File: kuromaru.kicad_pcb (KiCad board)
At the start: 2 copper layers, 134 x 95.1 mm, 78 parts, among them J1 USB_C_Receptacle_USB2.0, J108 Conn_01x01_Female, J109 Conn_01x01_Female, J5 Conn_01x02, SW1 SW_Push, SW101 SW_Push, SW102 SW_Push, SW103 SW_Push, SW104 SW_Push, SW105 SW_Push, SW106 SW_Push, SW107 SW_Push, SW108 SW_Push, SW109 SW_Push, SW110 SW_SPST_TL3342, SW112 SW_Push, SW113 SW_Push, SW114 SW_Push, SW115 SW_Push, SW116 SW_Push, SW117 SW_Push, SW118 SW_Push, SW119 locked, SW2 SW_Push, U1 RP2040, U2 GD25Q80CEIGR, U3 XC6210B332MR-G, Y1 Crystal_GND24

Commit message: Before diodeless design
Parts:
- removed J108, J109: Conn_01x01_Female, Connector_Wire:SolderWirePad_1x01_SMD_1x2mm
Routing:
- net rgb_l: track 7.18 -> 4.99 mm, vias 1 -> 0
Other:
- board text removed: "0"
- board text removed: "GPIO"

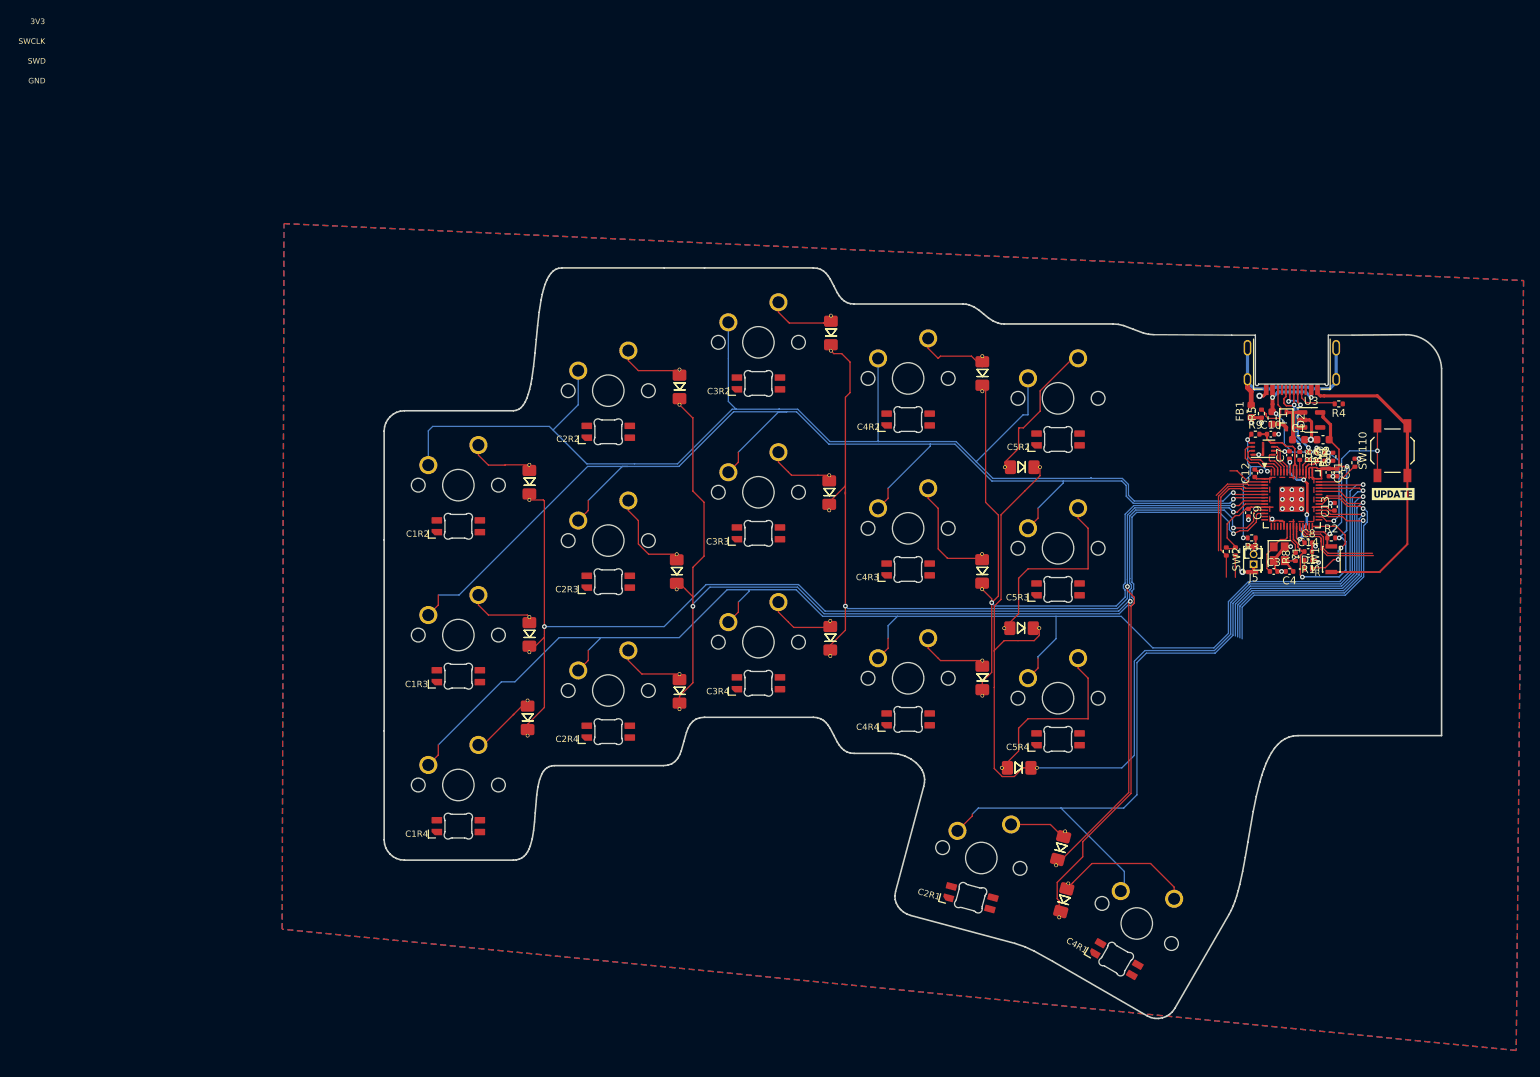
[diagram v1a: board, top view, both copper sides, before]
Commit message: Update to diodeless
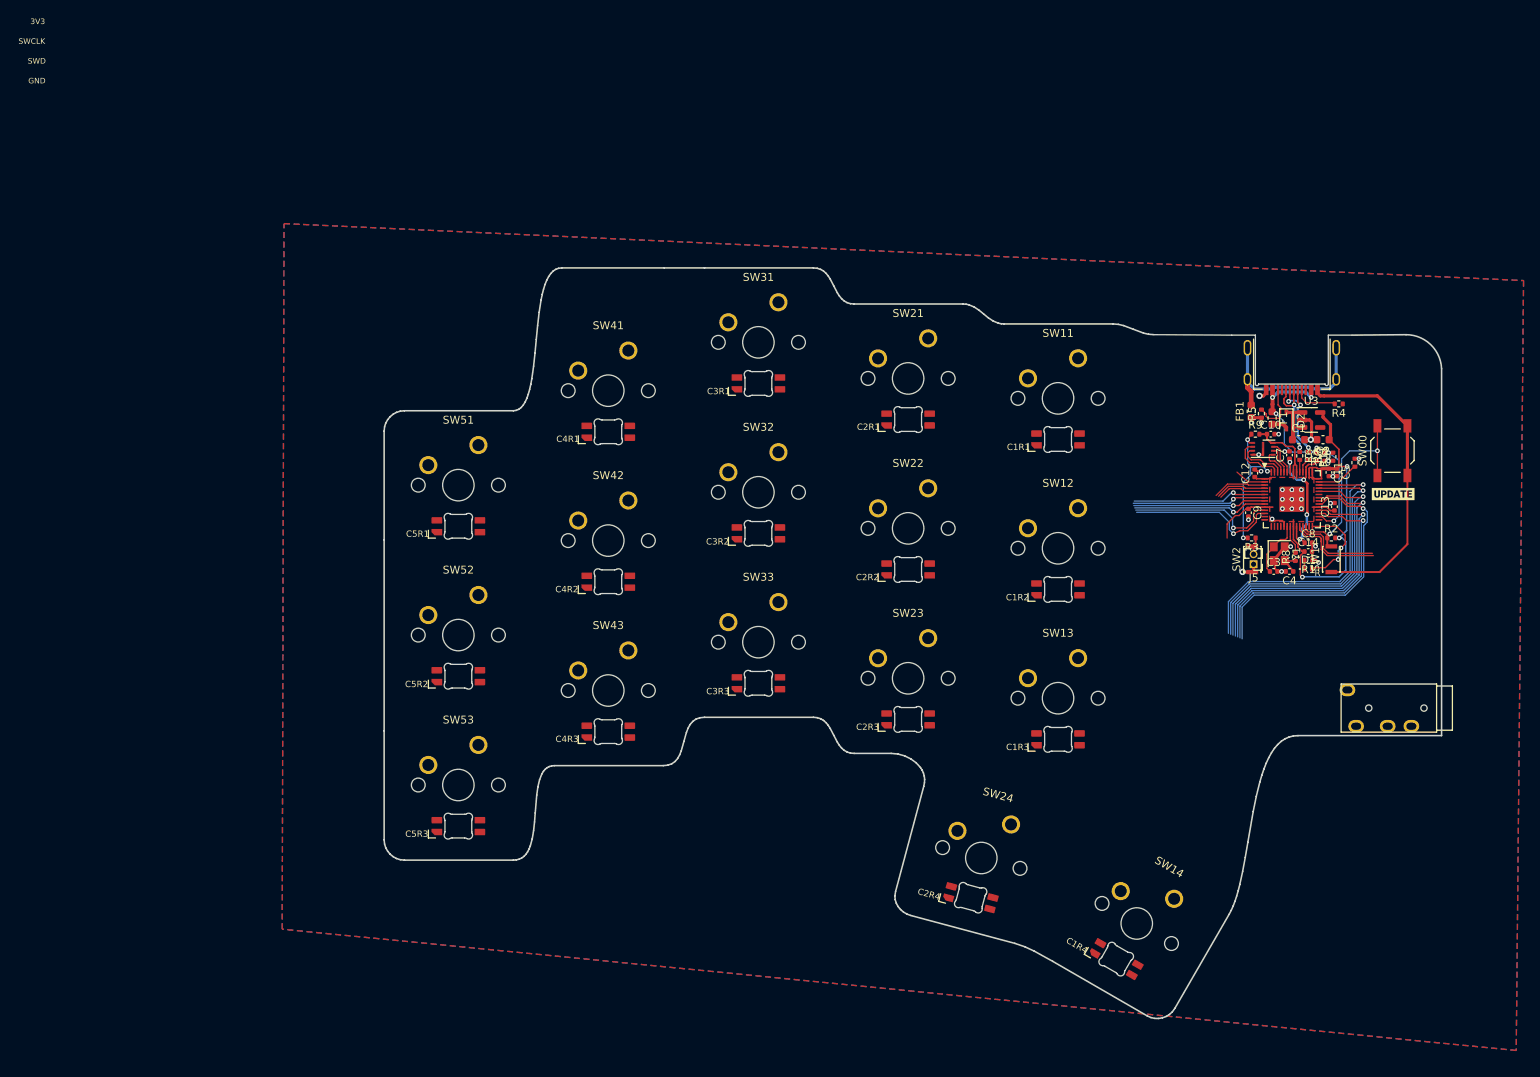
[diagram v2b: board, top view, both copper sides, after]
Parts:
- removed D101, D102, D103, D104, D105, D106, D107, D108, D109, D110, D111, D112, D113, D114, D115, D116, D117: D, local-libraries:D_1206_handsolder_reversible
- removed R103, R104: 4.7k, local-libraries:R_0402_1005Metric_nolabel
- added J102: Serial, keebio:TRRS-PJ-320A-no-Fmask, F.Cu at (177.4, 82.0)
- SW00: renamed from SW110; value SW_SPST_TL3342 -> SW_SPST
- SW11: renamed from SW115; value SW_Push -> SW_Push_SK6812
- SW12: renamed from SW116; value SW_Push -> SW_Push_SK6812
- SW13: renamed from SW117; value SW_Push -> SW_Push_SK6812
- SW21: renamed from SW112; value SW_Push -> SW_Push_SK6812
- SW22: renamed from SW113; value SW_Push -> SW_Push_SK6812
- SW23: renamed from SW114; value SW_Push -> SW_Push_SK6812
- SW24: renamed from SW118; value SW_Push -> SW_Push_SK6812
- SW31: renamed from SW107; value SW_Push -> SW_Push_SK6812
- SW32: renamed from SW108; value SW_Push -> SW_Push_SK6812
- SW33: renamed from SW109; value SW_Push -> SW_Push_SK6812
- SW41: renamed from SW104; value SW_Push -> SW_Push_SK6812
- SW42: renamed from SW105; value SW_Push -> SW_Push_SK6812
- SW43: renamed from SW106; value SW_Push -> SW_Push_SK6812
- SW51: renamed from SW101; value SW_Push -> SW_Push_SK6812
- SW52: renamed from SW102; value SW_Push -> SW_Push_SK6812
- SW53: renamed from SW103; value SW_Push -> SW_Push_SK6812
- renumbered SW119 to SW14
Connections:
- net NCS renamed /D21
- net miso_l renamed /MISO
- net mosi_l renamed /MOSI
- net rgb_l renamed rgb_din
- net sc_l renamed /SCLK
- net serial_l renamed serial_tx
- C1 pad 1: bat_l -> +5V
- C1 pad 2: Gnd_l -> GND
- C10 pad 2: Gnd_l -> GND
- C11 pad 2: Gnd_l -> GND
- C12 pad 2: Gnd_l -> GND
- C13 pad 2: Gnd_l -> GND
- C14 pad 2: Gnd_l -> GND
- C2 pad 2: Gnd_l -> GND
- C3 pad 2: Gnd_l -> GND
- C4 pad 2: Gnd_l -> GND
- C5 pad 2: Gnd_l -> GND
- C6 pad 2: Gnd_l -> GND
- C7 pad 2: Gnd_l -> GND
- C8 pad 2: Gnd_l -> GND
- C9 pad 2: Gnd_l -> GND
- D2 pad 1: bat_l -> +5V
- FB1 pad 1: Gnd_l -> GND
- J1 pad A1: Gnd_l -> GND
- J1 pad A12: Gnd_l -> GND
- J1 pad B1: Gnd_l -> GND
- J1 pad B12: Gnd_l -> GND
- J5 pad 1: Gnd_l -> GND
- R1 pad 1: Gnd_l -> GND
- R101 pad 2: Net-(JP111-Pad1) -> unconnected-(R101-Pad2)
- R11 pad 1: Gnd_l -> GND
- R4 pad 1: Gnd_l -> GND
- R5 pad 1: Gnd_l -> GND
- SW1 pad 1: Gnd_l -> unconnected-(SW1-Pad1)
- SW1 pad 2: Rst_l -> unconnected-(SW1-Pad2)
- SW11 pad 1: row2_l -> +5V
- SW11 pad 2: Net-(D113-Pad2) -> Net-(SW52-Pad4)
- SW11 pad 3: (no net) -> GND
- SW11 pad 4: (no net) -> Net-(SW11-Pad4)
- SW11 pad 5: (no net) -> GND
- SW11 pad 6: (no net) -> switch11
- SW12 pad 1: row3_l -> +5V
- SW12 pad 2: Net-(D114-Pad2) -> Net-(SW53-Pad4)
- SW12 pad 3: (no net) -> GND
- SW12 pad 4: (no net) -> Net-(SW12-Pad4)
- SW12 pad 5: (no net) -> GND
- SW12 pad 6: (no net) -> switch12
- SW13 pad 1: row4_l -> +5V
- SW13 pad 2: Net-(D115-Pad2) -> Net-(SW24-Pad4)
- SW13 pad 3: (no net) -> GND
- SW13 pad 4: (no net) -> Net-(SW13-Pad4)
- SW13 pad 5: (no net) -> GND
- SW13 pad 6: (no net) -> switch13
- SW14 pad 1: row1_l -> +5V
- SW14 pad 2: Net-(D117-Pad2) -> unconnected-(SW14-Pad2)
- SW14 pad 3: (no net) -> GND
- SW14 pad 4: (no net) -> Net-(SW14-Pad4)
- SW14 pad 5: (no net) -> GND
- SW14 pad 6: (no net) -> switch14
- SW2 pad 1: Gnd_l -> unconnected-(SW2-Pad1)
- SW2 pad 2: Net-(J5-Pad2) -> unconnected-(SW2-Pad2)
- SW21 pad 1: row2_l -> +5V
- SW21 pad 2: Net-(D110-Pad2) -> Net-(SW11-Pad4)
- SW21 pad 3: (no net) -> GND
- SW21 pad 4: (no net) -> Net-(SW21-Pad4)
- SW21 pad 5: (no net) -> GND
- SW21 pad 6: (no net) -> switch21
- SW22 pad 1: row3_l -> +5V
- SW22 pad 2: Net-(D111-Pad2) -> Net-(SW12-Pad4)
- SW22 pad 3: (no net) -> GND
- SW22 pad 4: (no net) -> Net-(SW22-Pad4)
- SW22 pad 5: (no net) -> GND
- SW22 pad 6: (no net) -> switch22
- SW23 pad 1: row4_l -> +5V
- SW23 pad 2: Net-(D112-Pad2) -> Net-(SW13-Pad4)
- SW23 pad 3: (no net) -> GND
- SW23 pad 4: (no net) -> Net-(SW23-Pad4)
- SW23 pad 5: (no net) -> GND
- SW23 pad 6: (no net) -> switch23
- SW24 pad 1: row1_l -> +5V
- SW24 pad 2: Net-(D116-Pad2) -> Net-(SW14-Pad4)
- SW24 pad 3: (no net) -> GND
- SW24 pad 4: (no net) -> Net-(SW24-Pad4)
- SW24 pad 5: (no net) -> GND
- SW24 pad 6: (no net) -> switch24
- SW31 pad 1: row2_l -> +5V
- SW31 pad 2: Net-(D107-Pad2) -> Net-(SW21-Pad4)
- SW31 pad 3: (no net) -> GND
- SW31 pad 4: (no net) -> Net-(SW31-Pad4)
- SW31 pad 5: (no net) -> GND
- SW31 pad 6: (no net) -> switch31
- SW32 pad 1: row3_l -> +5V
- SW32 pad 2: Net-(D108-Pad2) -> Net-(SW22-Pad4)
- SW32 pad 3: (no net) -> GND
- SW32 pad 4: (no net) -> Net-(SW32-Pad4)
- SW32 pad 5: (no net) -> GND
- SW32 pad 6: (no net) -> switch32
- SW33 pad 1: row4_l -> +5V
- SW33 pad 2: Net-(D109-Pad2) -> Net-(SW23-Pad4)
- SW33 pad 3: (no net) -> GND
- SW33 pad 4: (no net) -> Net-(SW33-Pad4)
- SW33 pad 5: (no net) -> GND
- SW33 pad 6: (no net) -> switch33
- SW41 pad 1: row2_l -> +5V
- SW41 pad 2: Net-(D104-Pad2) -> Net-(SW31-Pad4)
- SW41 pad 3: (no net) -> GND
- SW41 pad 4: (no net) -> Net-(SW41-Pad4)
- SW41 pad 5: (no net) -> GND
- SW41 pad 6: (no net) -> switch41
- SW42 pad 1: row3_l -> +5V
- SW42 pad 2: Net-(D105-Pad2) -> Net-(SW32-Pad4)
- SW42 pad 3: (no net) -> GND
- SW42 pad 4: (no net) -> Net-(SW42-Pad4)
- SW42 pad 5: (no net) -> GND
- SW42 pad 6: (no net) -> switch42
- SW43 pad 1: row4_l -> +5V
- SW43 pad 2: Net-(D106-Pad2) -> Net-(SW33-Pad4)
- SW43 pad 3: (no net) -> GND
- SW43 pad 4: (no net) -> Net-(SW53-Pad2)
- SW43 pad 5: (no net) -> GND
- SW43 pad 6: (no net) -> switch43
- SW51 pad 1: row2_l -> +5V
- SW51 pad 2: Net-(D101-Pad2) -> Net-(SW41-Pad4)
- SW51 pad 3: (no net) -> GND
- SW51 pad 4: (no net) -> Net-(SW51-Pad4)
- SW51 pad 5: (no net) -> GND
- SW51 pad 6: (no net) -> switch51
- SW52 pad 1: row3_l -> +5V
- SW52 pad 2: Net-(D102-Pad2) -> Net-(SW42-Pad4)
- SW52 pad 3: (no net) -> GND
- SW52 pad 4: (no net) -> Net-(SW52-Pad4)
- SW52 pad 5: (no net) -> GND
- SW52 pad 6: (no net) -> switch52
- SW53 pad 1: row4_l -> +5V
- SW53 pad 2: Net-(D103-Pad2) -> Net-(SW53-Pad2)
- SW53 pad 3: (no net) -> GND
- SW53 pad 4: (no net) -> Net-(SW53-Pad4)
- SW53 pad 5: (no net) -> GND
- SW53 pad 6: (no net) -> switch53
- U1 pad 11: col1_l -> switch21
- U1 pad 12: col2_l -> switch22
- U1 pad 13: unconnected-(U1-Pad13) -> switch23
- U1 pad 14: unconnected-(U1-Pad14) -> switch24
- U1 pad 15: /D12 -> switch25
- U1 pad 16: /D13 -> switch21
- U1 pad 17: /D14 -> switch22
- U1 pad 18: /D15 -> switch23
- U1 pad 19: Gnd_l -> GND
- U1 pad 27: /D16 -> switch24
- U1 pad 29: unconnected-(U1-Pad29) -> switch25
- U1 pad 36: unconnected-(U1-Pad36) -> switch24
- U1 pad 37: unconnected-(U1-Pad37) -> switch25
- U1 pad 38: row1_l -> /A0
- U1 pad 39: col5_l -> /A1
- U1 pad 4: sda_l -> serial_rx
- U1 pad 40: row4_l -> /A2
- U1 pad 41: hand -> /A3
- U1 pad 5: scl_l -> switch11
- U1 pad 57: Gnd_l -> GND
- U1 pad 6: row2_l -> switch12
- U1 pad 7: row3_l -> switch13
- U1 pad 8: col4_l -> switch14
- U1 pad 9: col3_l -> switch15
- U2 pad 4: Gnd_l -> GND
- U2 pad 9: Gnd_l -> GND
- U3 pad 1: bat_l -> +5V
- U3 pad 2: Gnd_l -> GND
- U3 pad 3: bat_l -> +5V
- Y1 pad 2: Gnd_l -> GND
- Y1 pad 4: Gnd_l -> GND
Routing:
- net col1_l: track 182.8 -> 0.00 mm, vias 3 -> 0
- net row4_l: track 180.1 -> 0.00 mm, vias 1 -> 0
- net row2_l: track 166.4 -> 0.00 mm, vias 1 -> 0
- net row3_l: track 163.1 -> 0.00 mm, vias 1 -> 0
- net col3_l: track 157.7 -> 0.00 mm, vias 3 -> 0
- net col2_l: track 134.7 -> 0.00 mm, vias 2 -> 0
- net col5_l: track 130.9 -> 0.00 mm, vias 1 -> 0
- net row1_l: track 107.2 -> 0.00 mm, vias 1 -> 0
- net col4_l: track 90.3 -> 0.00 mm, vias 2 -> 0
- net Gnd_l: track 69.8 -> 0.00 mm, vias 27 -> 11
- net GND: track 0.00 -> 67.5 mm, vias 0 -> 15
- net /A2: track 0.00 -> 38.8 mm, vias 0 -> 1
- net /A1: track 0.00 -> 38.0 mm, vias 0 -> 1
- net /A0: track 0.00 -> 37.3 mm, vias 0 -> 1
- net Net-(D114-Pad2): track 24.6 -> 0.00 mm
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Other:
- board text added: "C1R1"
- board text added: "C3R1"
- board text added: "C5R1"
- board text removed: "C3R4"
- board text removed: "C4R4"
- board text removed: "C5R4"

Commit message: Rework controller, commit before splay
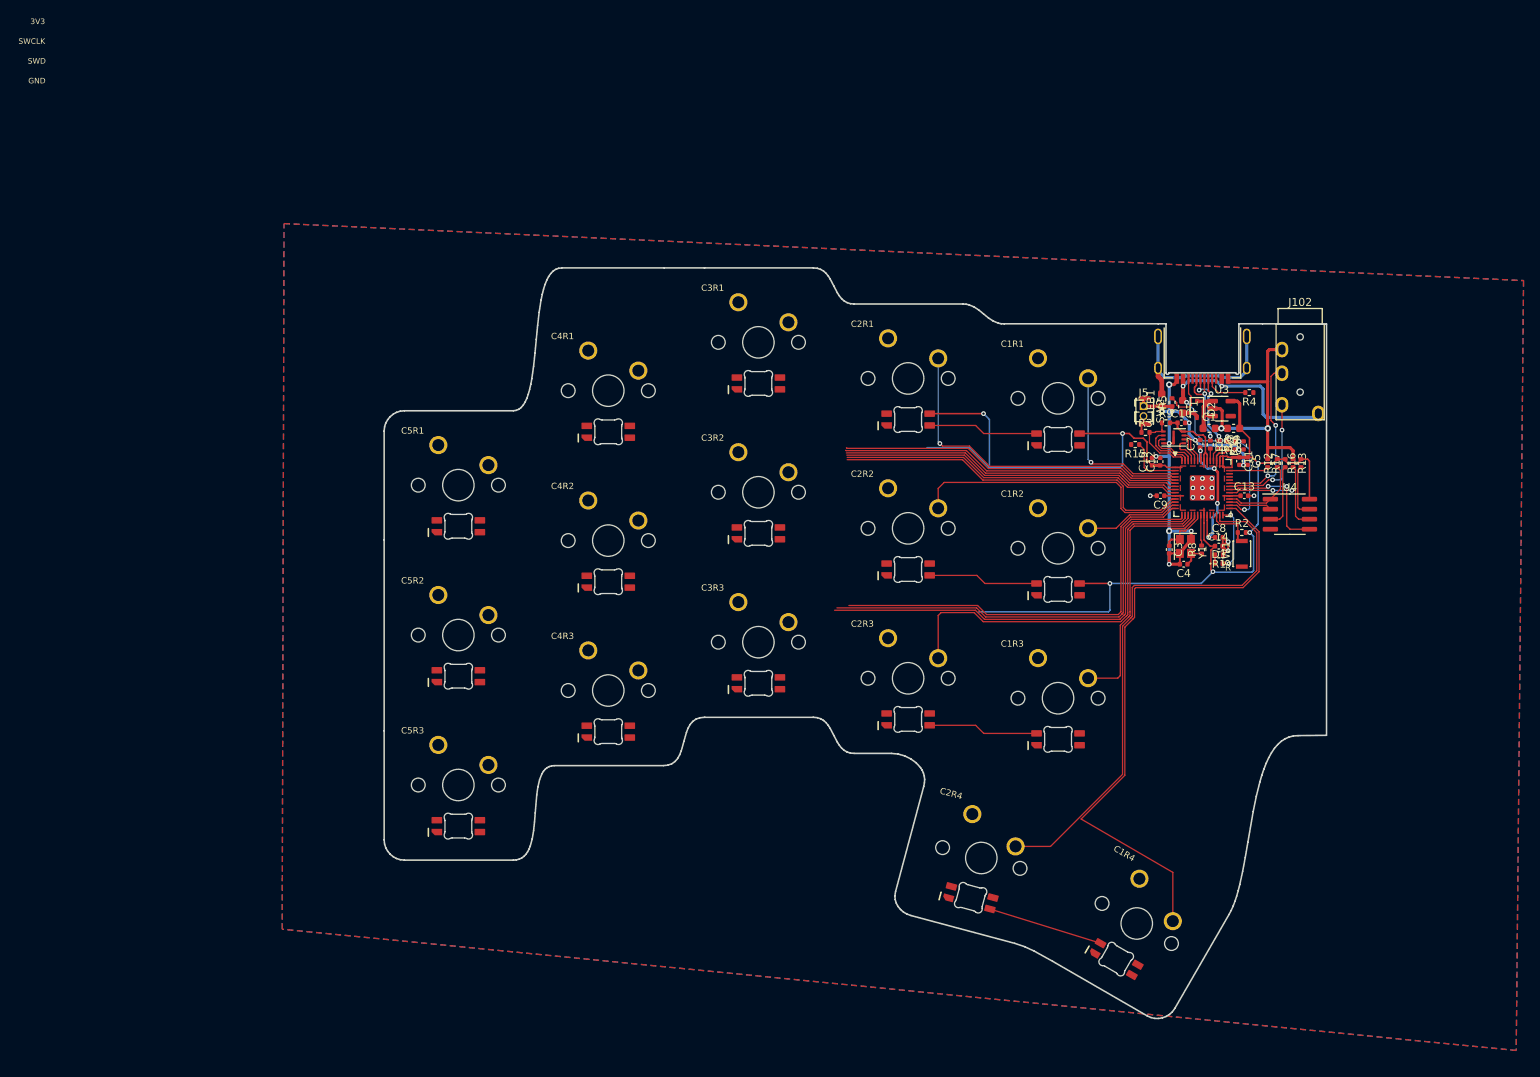
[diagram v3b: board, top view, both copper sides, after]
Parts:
- removed SW00: SW_SPST, Button_Switch_SMD:SW_SPST_TL3342
- removed kibuzzard-62C19A64: G***, kibuzzard-62C19A64
- added C15: 1µ, Capacitor_SMD:C_0402_1005Metric, F.Cu at (141.4, 50.8)
- added R12: 100k, Resistor_SMD:R_0402_1005Metric, F.Cu at (157.2, 51.0)
- added R13: 100k, Resistor_SMD:R_0402_1005Metric, F.Cu at (159.2, 51.0)
- added R15: 300, Resistor_SMD:R_0402_1005Metric, F.Cu at (139.2, 48.6)
- added R16: 5.1k, Resistor_SMD:R_0402_1005Metric, F.Cu at (160.2, 51.0)
- added R17: 5.1k, Resistor_SMD:R_0402_1005Metric, F.Cu at (158.2, 51.0)
- added U4: 25LCxxx, Package_SO:SOIC-8_3.9x4.9mm_P1.27mm, F.Cu at (158.8, 57.4)
- J102: footprint keebio:TRRS-PJ-320A-no-Fmask -> local-libraries:delay_TRRS_PJ_320A
- moved J102 46.9 mm to (160.1, 38.4), turned to 0 degrees
- moved J5 24.4 mm to (140.3, 43.7), turned to 0 degrees
- moved SW2 23.2 mm to (140.4, 44.4), turned to -90 degrees
- moved R3 19.0 mm to (140.5, 47.1), turned to 0 degrees
- moved C3 13.5 mm to (143.5, 61.9), turned to -90 degrees
- moved C4 13.4 mm to (145.3, 63.8)
- moved C12 12.1 mm to (142.4, 50.8)
- moved R8 11.9 mm to (147.6, 61.9)
- moved Y1 11.9 mm to (145.6, 61.5)
- moved C13 11.5 mm to (153.0, 55.1), turned to 0 degrees
- moved C1 11.4 mm to (148.6, 46.5)
- moved C2 11.4 mm to (151.7, 46.5)
- moved C6 11.4 mm to (151.4, 49.2)
- moved C7 11.4 mm to (147.4, 48.5)
- moved F1 11.4 mm to (145.2, 43.8)
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- renumbered SW11 to C1R1, SW12 to C1R2, SW13 to C1R3, SW14 to C1R4, SW21 to C2R1, SW22 to C2R2, SW23 to C2R3, SW24 to C2R4, SW31 to C3R1, SW32 to C3R2, SW33 to C3R3, SW41 to C4R1, SW42 to C4R2, SW43 to C4R3, SW51 to C5R1, SW52 to C5R2, SW53 to C5R3, R101 to R14
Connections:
- C1R1 pad 1: +5V -> +3V3
- C1R1 pad 6: switch11 -> switch_c1r1
- C1R2 pad 1: +5V -> +3V3
- C1R2 pad 6: switch12 -> switch_c1r2
- C1R3 pad 1: +5V -> +3V3
- C1R3 pad 6: switch13 -> switch_c1r3
- C1R4 pad 1: +5V -> +3V3
- C1R4 pad 6: switch14 -> switch_c1r4
- C2R1 pad 1: +5V -> +3V3
- C2R1 pad 6: switch21 -> switch_c2r1
- C2R2 pad 1: +5V -> +3V3
- C2R2 pad 6: switch22 -> switch_c2r2
- C2R3 pad 1: +5V -> +3V3
- C2R3 pad 6: switch23 -> switch_c2r3
- C2R4 pad 1: +5V -> +3V3
- C2R4 pad 6: switch24 -> switch_c2r4
- C3R1 pad 1: +5V -> +3V3
- C3R1 pad 6: switch31 -> switch_c3r1
- C3R2 pad 1: +5V -> +3V3
- C3R2 pad 6: switch32 -> switch_c3r2
- C3R3 pad 1: +5V -> +3V3
- C3R3 pad 6: switch33 -> switch_c3r3
- C4R1 pad 1: +5V -> +3V3
- C4R1 pad 6: switch41 -> switch_c4r1
- C4R2 pad 1: +5V -> +3V3
- C4R2 pad 6: switch42 -> switch_c4r2
- C4R3 pad 1: +5V -> +3V3
- C4R3 pad 6: switch43 -> switch_c4r3
- C5R1 pad 1: +5V -> +3V3
- C5R1 pad 6: switch51 -> switch_c5r1
- C5R2 pad 1: +5V -> +3V3
- C5R2 pad 6: switch52 -> switch_c5r2
- C5R3 pad 1: +5V -> +3V3
- C5R3 pad 6: switch53 -> switch_c5r3
- R14 pad 1: hand -> hands
- R14 pad 2: unconnected-(R101-Pad2) -> GND
- R2 pad 1: Rst_l -> reset
- SW1 pad 1: unconnected-(SW1-Pad1) -> GND
- SW1 pad 2: unconnected-(SW1-Pad2) -> reset
- SW2 pad 1: unconnected-(SW2-Pad1) -> GND
- SW2 pad 2: unconnected-(SW2-Pad2) -> Net-(J5-Pad2)
- U1 pad 11: switch21 -> switch_c3r2
- U1 pad 12: switch22 -> switch_c2r2
- U1 pad 13: switch23 -> switch_c1r2
- U1 pad 14: switch24 -> switch_c5r3
- U1 pad 15: switch25 -> switch_c4r3
- U1 pad 16: switch21 -> switch_c3r3
- U1 pad 17: switch22 -> switch_c2r3
- U1 pad 18: switch23 -> switch_c1r3
- U1 pad 26: Rst_l -> reset
- U1 pad 27: switch24 -> switch_c2r4
- U1 pad 29: switch25 -> switch_c1r4
- U1 pad 3: serial_tx -> switch_c1r1
- U1 pad 32: /D21 -> /EEPROM_CS
- U1 pad 36: switch24 -> serial_tx
- U1 pad 37: switch25 -> serial_rx
- U1 pad 4: serial_rx -> switch_c2r1
- U1 pad 41: /A3 -> hands
- U1 pad 5: switch11 -> switch_c3r1
- U1 pad 6: switch12 -> switch_c4r1
- U1 pad 7: switch13 -> switch_c5r1
- U1 pad 8: switch14 -> switch_c5r2
- U1 pad 9: switch15 -> switch_c4r2
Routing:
- net +3V3: track 72.2 -> 174.6 mm, vias 3 -> 6
- net switch_c1r4: track 0.00 -> 78.3 mm
- net switch_c2r4: track 0.00 -> 69.1 mm
- net switch_c3r3: track 0.00 -> 56.9 mm
- net switch_c4r3: track 0.00 -> 56.1 mm
- net switch_c5r3: track 0.00 -> 53.7 mm
- net switch_c2r3: track 0.00 -> 49.9 mm
- net GND: track 67.5 -> 114.3 mm, vias 15 -> 27
- net switch_c3r2: track 0.00 -> 46.4 mm
- net switch_c4r1: track 0.00 -> 43.5 mm
- net switch_c5r1: track 0.00 -> 43.4 mm
- net switch_c5r2: track 0.00 -> 43.4 mm
- net switch_c4r2: track 0.00 -> 43.4 mm
- net switch_c3r1: track 0.00 -> 43.4 mm
- net switch_c2r1: track 0.00 -> 42.5 mm, vias 0 -> 1
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- added copper zone on B.Cu, net GND
- added copper zone on F.Cu, net GND
- removed copper zone on B.Cu, net Gnd_l
- removed copper zone on F.Cu, net Gnd_l
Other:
- board size 134 x 95.1 mm -> 119.4 x 95.1 mm
- board text removed: "C1R1"
- board text removed: "C1R2"
- board text removed: "C1R3"
- board text removed: "C1R4"
- board text removed: "C2R1"
- board text removed: "C2R2"
- board text removed: "C2R3"
- board text removed: "C2R4"
- board text removed: "C3R1"
- board text removed: "C3R2"
- board text removed: "C3R3"
- board text removed: "C4R1"
- board text removed: "C4R2"
- board text removed: "C4R3"
- board text removed: "C5R1"
- board text removed: "C5R2"
- board text removed: "C5R3"

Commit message: Post splay
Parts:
- moved C5R1 5.69 mm to (48.6, 56.8), turned to 7.5 degrees
- moved C4R1 3.98 mm to (68.6, 42.8), turned to 5 degrees
- moved C5R2 3.72 mm to (51.1, 75.7), turned to 7.5 degrees
- moved C5R3 2.76 mm to (53.6, 94.5), turned to 7.5 degrees
- moved C4R2 2.38 mm to (70.2, 61.7), turned to 5 degrees
- moved C3R1 2.09 mm to (89.4, 35.5), turned to 2.5 degrees
- moved C3R2 1.27 mm to (90.2, 54.5), turned to 2.5 degrees
- moved C4R3 1.00 mm to (71.9, 80.6), turned to 5 degrees
- moved C3R3 0.46 mm to (91.0, 73.5), turned to 2.5 degrees
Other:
- outline, holes or cut-outs redrawn
